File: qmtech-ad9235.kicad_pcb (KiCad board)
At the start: 4 copper layers, 60 x 45 mm, 49 parts

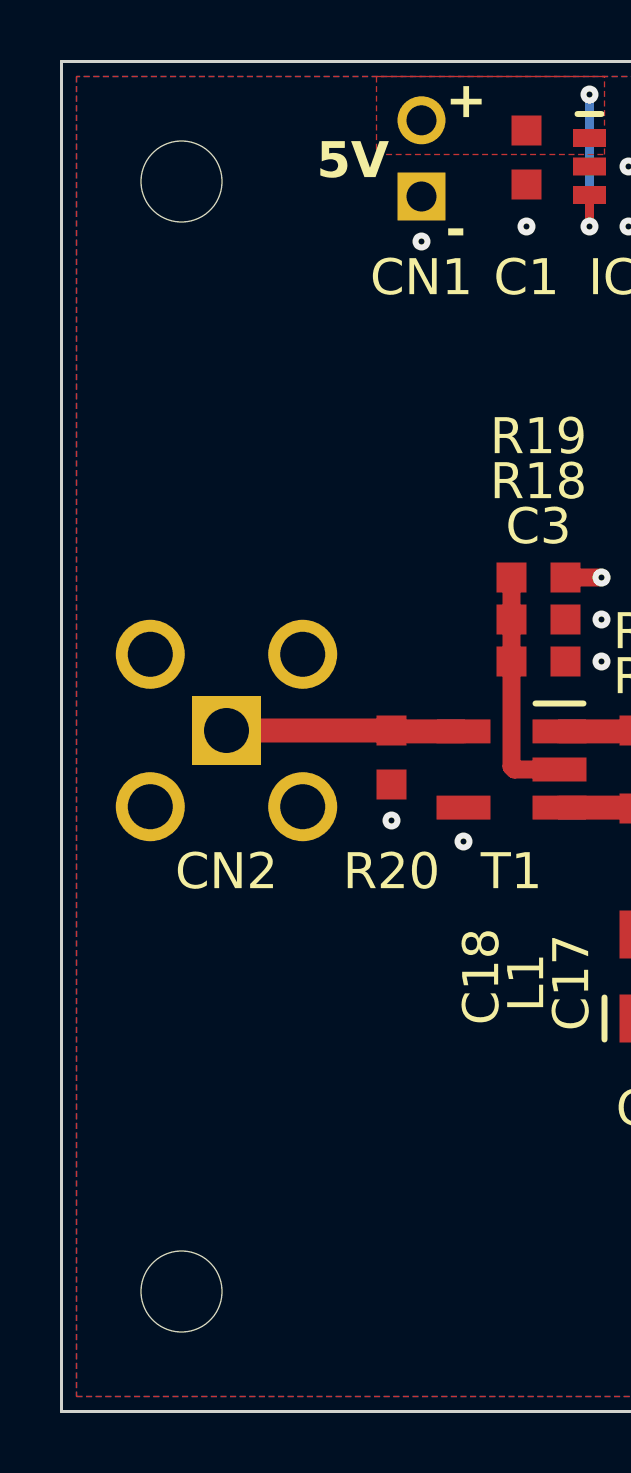
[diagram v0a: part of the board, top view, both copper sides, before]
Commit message: replace M25 with M3
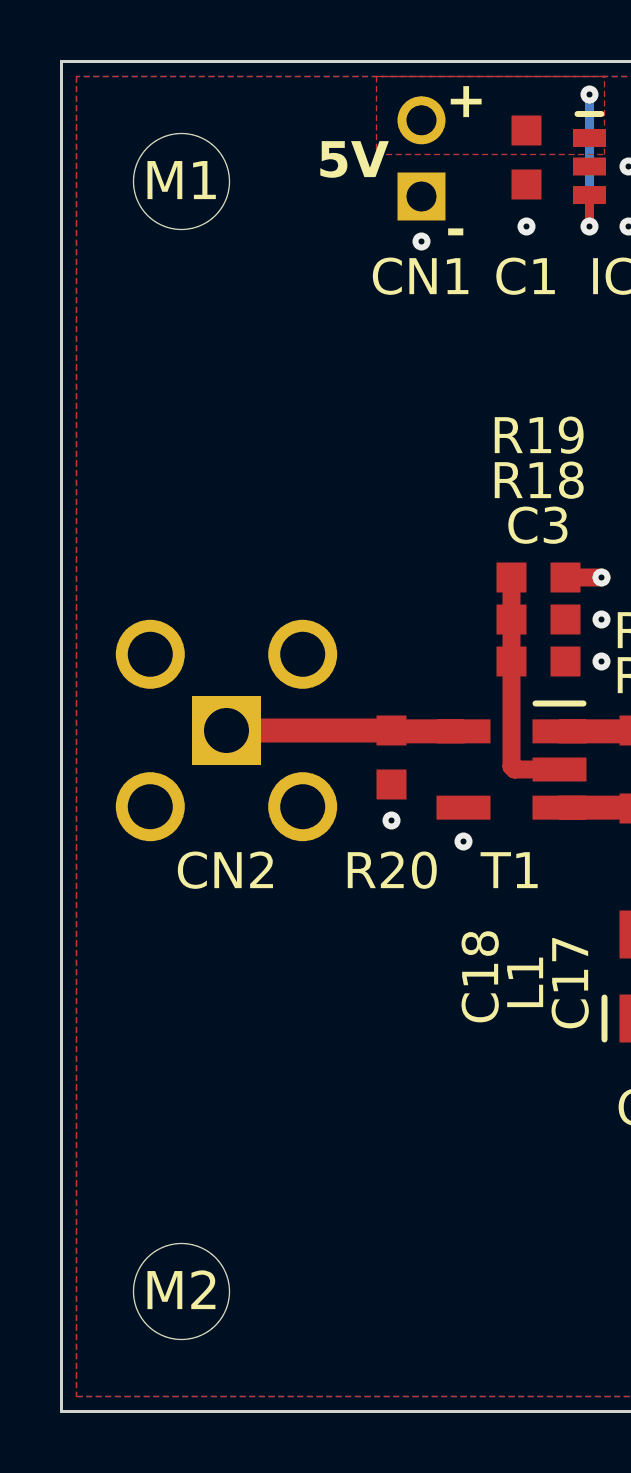
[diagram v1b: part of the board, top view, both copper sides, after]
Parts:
- M1, M2: footprint footprints:M25 -> footprints:M3
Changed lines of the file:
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@@
       (net 18 "GND"))
   )
-  (footprint "footprints:M25" (layer "F.Cu")
+  (footprint "footprints:M3" (layer "F.Cu")
     (at 72 52)
     (property "mpn" "hole")
     (clearance 1)
     (attr through_hole)
-    (fp_text reference "M1" (at 0 0) (layer "F.SilkS") hide
+    (fp_text reference "M1" (at 0 0) (layer "F.SilkS")
         (effects (font (size 1.27 1.27) (thickness 0.15)))
     )
@@
         (effects (font (size 1.27 1.27) (thickness 0.15)))
     )
-    (pad "" np_thru_hole circle (at 0 0) (size 2.7 2.7) (drill 2.7) (layers "*.Cu" "*.Mask"))
+    (pad "" np_thru_hole circle (at 0 0) (size 3.2 3.2) (drill 3.2) (layers "*.Cu" "*.Mask"))
   )
   (footprint "footprints:0603" (layer "F.Cu")
@@
       (net 18 "GND"))
   )
-  (footprint "footprints:M25" (layer "F.Cu")
+  (footprint "footprints:M3" (layer "F.Cu")
     (at 72 89)
     (property "mpn" "hole")
     (clearance 1)
     (attr through_hole)
-    (fp_text reference "M2" (at 0 0) (layer "F.SilkS") hide
+    (fp_text reference "M2" (at 0 0) (layer "F.SilkS")
         (effects (font (size 1.27 1.27) (thickness 0.15)))
     )
-    (fp_text value "" (at 0 0) (layer "F.SilkS") hide
+    (fp_text value "" (at 0 0) (layer "F.SilkS")
         (effects (font (size 1.27 1.27) (thickness 0.15)))
     )
-    (pad "" np_thru_hole circle (at 0 0) (size 2.7 2.7) (drill 2.7) (layers "*.Cu" "*.Mask"))
+    (pad "" np_thru_hole circle (at 0 0) (size 3.2 3.2) (drill 3.2) (layers "*.Cu" "*.Mask"))
   )
   (footprint "footprints:1x17" (layer "F.Cu")

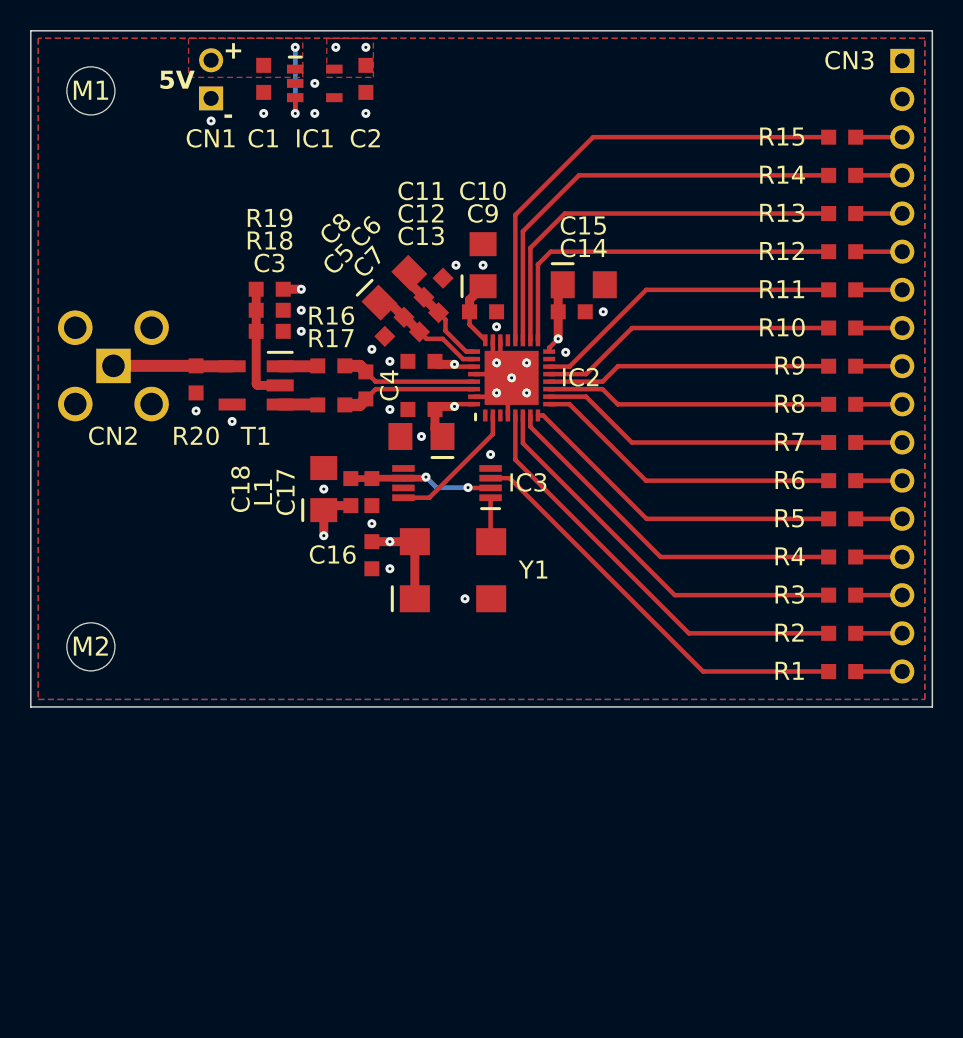
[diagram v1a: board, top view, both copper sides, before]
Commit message: reduce length of output traces
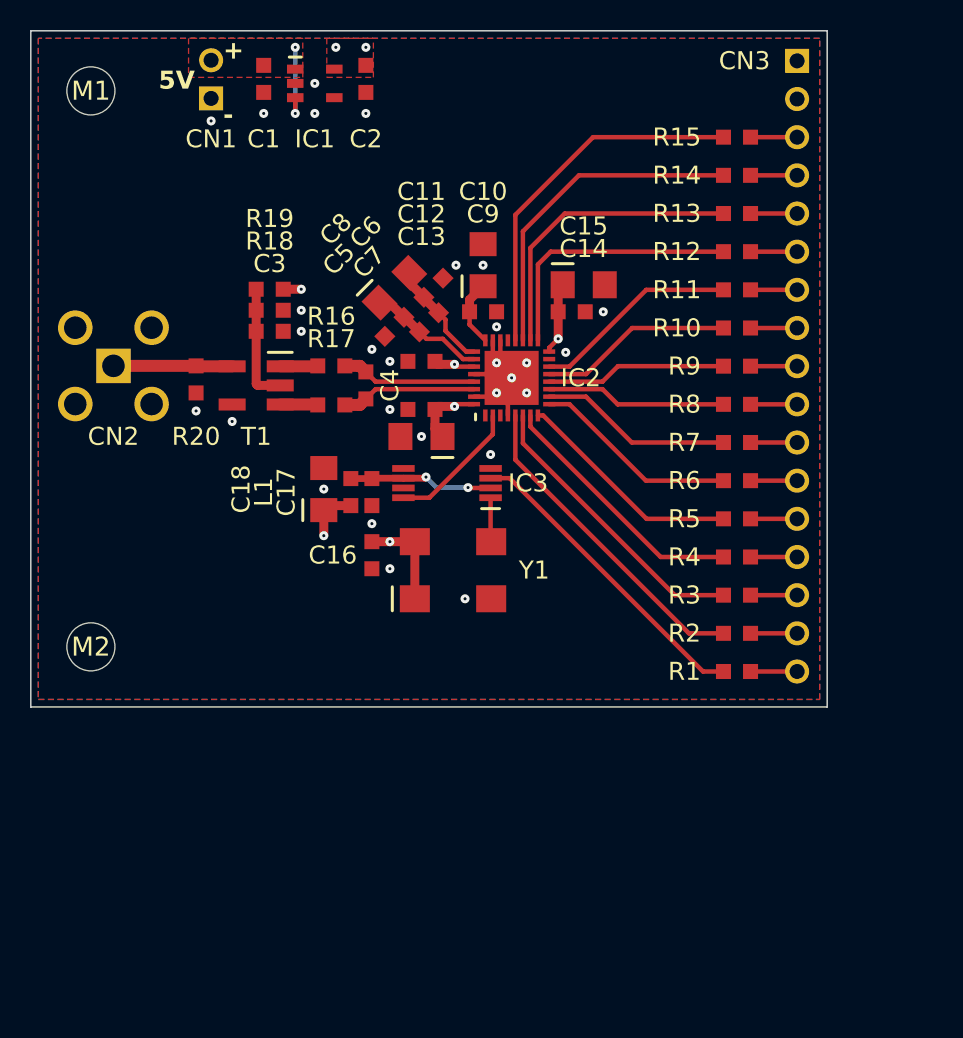
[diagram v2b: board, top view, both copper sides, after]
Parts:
- moved CN3 7.00 mm to (119.0, 50.0)
- moved R1 7.00 mm to (115.0, 90.6)
- moved R10 7.00 mm to (115.0, 67.8)
- moved R11 7.00 mm to (115.0, 65.2)
- moved R12 7.00 mm to (115.0, 62.7)
- moved R13 7.00 mm to (115.0, 60.2)
- moved R14 7.00 mm to (115.0, 57.6)
- moved R15 7.00 mm to (115.0, 55.1)
- moved R2 7.00 mm to (115.0, 88.1)
- moved R3 7.00 mm to (115.0, 85.6)
- moved R4 7.00 mm to (115.0, 83.0)
- moved R5 7.00 mm to (115.0, 80.5)
- moved R6 7.00 mm to (115.0, 77.9)
- moved R7 7.00 mm to (115.0, 75.4)
- moved R8 7.00 mm to (115.0, 72.9)
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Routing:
- net D6: track 19.0 -> 12.0 mm
- net Y1: track 27.8 -> 20.8 mm
- net D8: track 19.9 -> 12.9 mm
- net D7: track 19.0 -> 12.0 mm
- net D5: track 19.9 -> 12.9 mm
- net D4: track 20.7 -> 13.7 mm
- net D3: track 22.2 -> 15.2 mm
- net D2: track 24.2 -> 17.2 mm
- net D13: track 31.3 -> 24.3 mm
- net D12: track 29.1 -> 22.1 mm
- net D11: track 26.9 -> 19.9 mm
- net D10: track 24.8 -> 17.8 mm
- net D1: track 26.4 -> 19.4 mm
- net D0: track 28.6 -> 21.6 mm
- net D9: track 20.7 -> 13.7 mm
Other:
- board size 60 x 45 mm -> 53 x 45 mm

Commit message: improve AVDD and GND connections
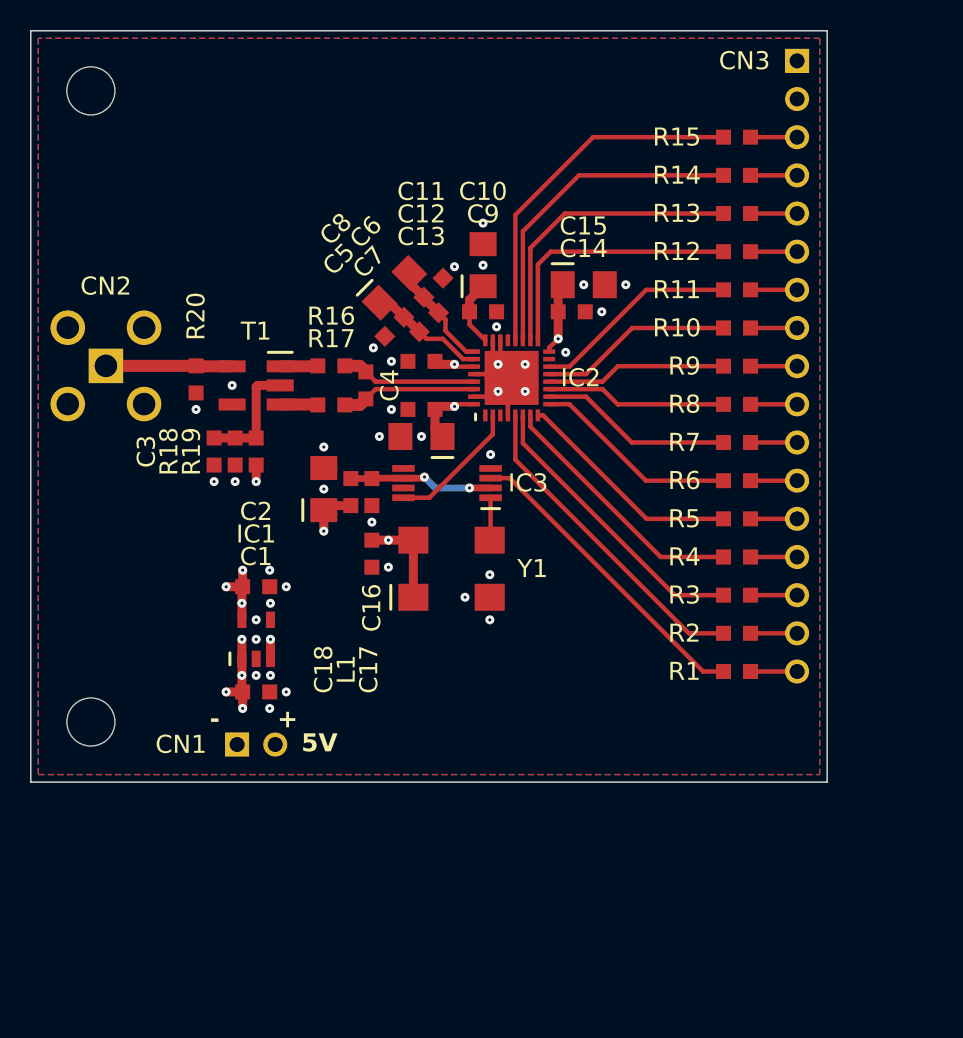
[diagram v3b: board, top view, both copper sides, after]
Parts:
- moved CN1 43.1 mm to (83.0, 95.5), turned to 0 degrees
- moved C1 40.8 mm to (83.0, 92.0), turned to 0 degrees
- moved IC1 37.2 mm to (83.0, 88.5), turned to 90 degrees
- moved C2 34.6 mm to (83.0, 85.0), turned to 0 degrees
- moved R18 10.8 mm to (83.0, 76.0), turned to 90 degrees
- moved R19 9.68 mm to (81.6, 76.0), turned to -90 degrees
- moved C3 8.81 mm to (80.2, 76.0), turned to -90 degrees
- moved M2 5.00 mm to (72.0, 94.0)
- moved CN2 0.50 mm to (73.0, 70.3)
- moved Y1 0.14 mm to (96.0, 83.8)
- moved C16 0.10 mm to (90.7, 82.8)
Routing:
- net AVDD: track 18.9 -> 22.9 mm, vias 7 -> 8
- net 5V: track 5.45 -> 7.02 mm, vias 2 -> 5
- net INPUT: track 7.91 -> 8.41 mm
- net GND: vias 28 -> 38
- added copper zone on In2.Cu, net 5V
- added copper zone on In2.Cu, net AVDD
- added copper zone on In2.Cu, net DVDD
- added copper zone on In1.Cu, net GND
- removed copper zone on F.Cu, net 5V
- removed copper zone on F.Cu, net AVDD
- removed copper zone on In1.Cu, net AVDD
- removed copper zone on In1.Cu, net DVDD
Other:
- board size 53 x 45 mm -> 53 x 50 mm

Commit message: replace 1x17 with 2x25
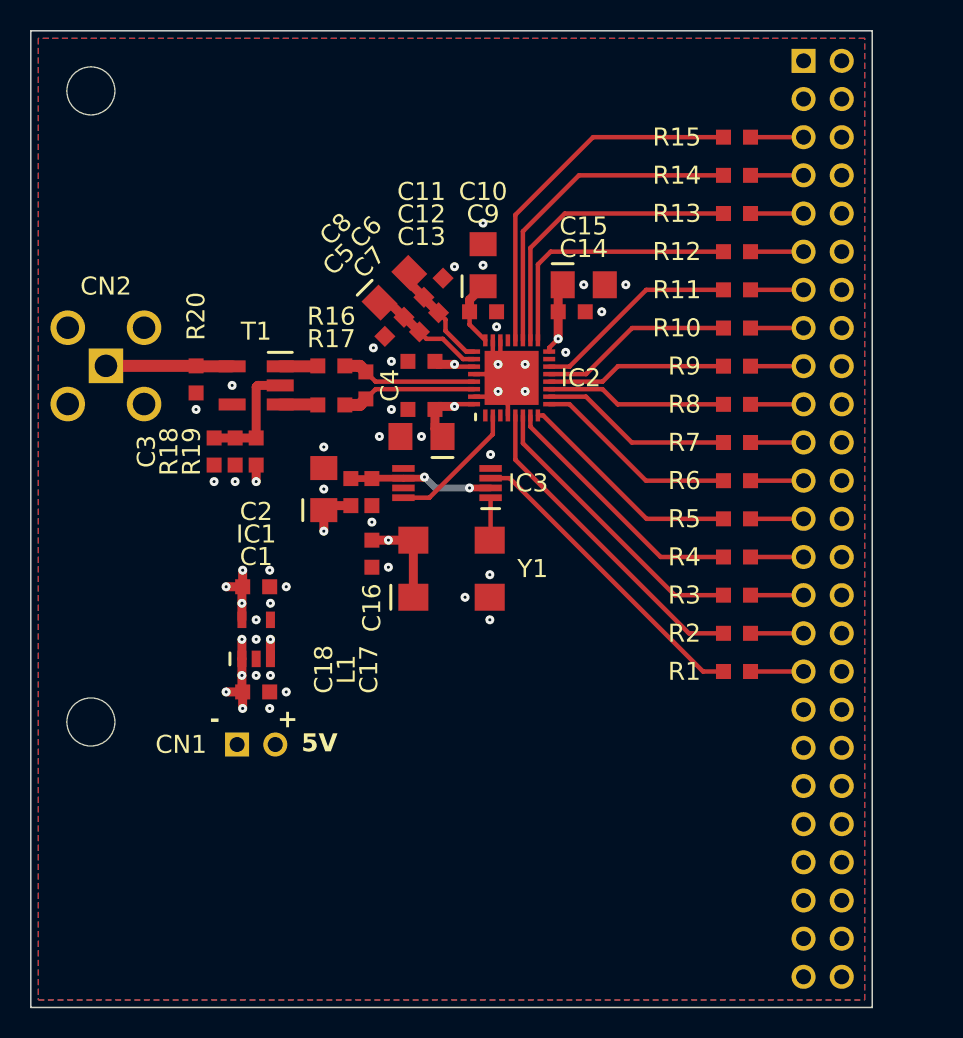
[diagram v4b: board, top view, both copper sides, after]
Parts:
- CN3: footprint footprints:1x17 -> footprints:2x25; moved to B.Cu
- moved CN3 1.70 mm to (120.7, 50.0)
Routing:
- net W9: track 3.00 -> 3.53 mm
- net W8: track 3.00 -> 3.53 mm
- net W7: track 3.00 -> 3.53 mm
- net W6: track 3.00 -> 3.53 mm
- net W5: track 3.00 -> 3.53 mm
- net W4: track 3.00 -> 3.53 mm
- net W3: track 3.00 -> 3.53 mm
- net W2: track 3.00 -> 3.53 mm
- net W15: track 3.00 -> 3.53 mm
- net W14: track 3.00 -> 3.53 mm
- net W13: track 3.00 -> 3.53 mm
- net W12: track 3.00 -> 3.53 mm
- net W11: track 3.00 -> 3.53 mm
- net W10: track 3.00 -> 3.53 mm
- net W1: track 3.00 -> 3.53 mm
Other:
- board size 53 x 50 mm -> 56 x 65 mm

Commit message: add DVDD regulator
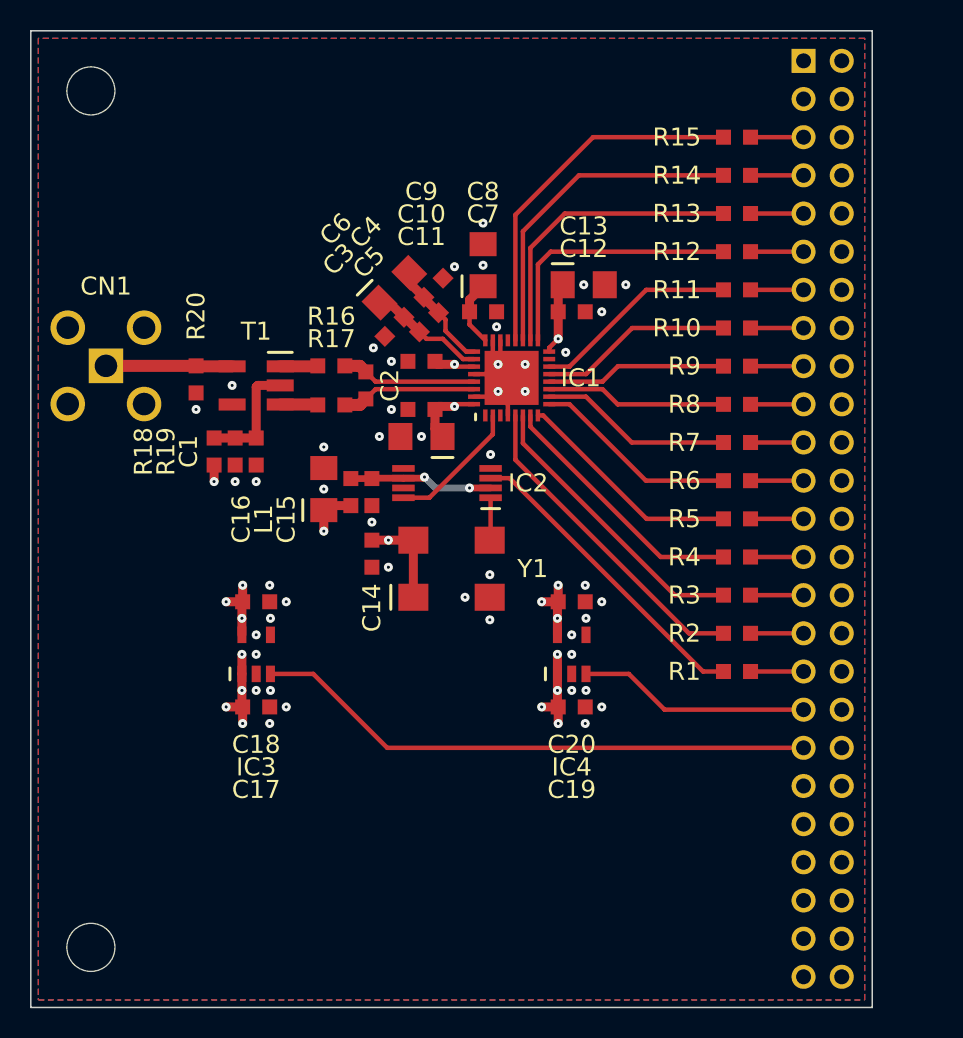
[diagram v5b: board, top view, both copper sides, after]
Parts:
- removed the CN1 at (83.0, 95.5)
- added C19: , footprints:0603, F.Cu at (104.0, 93.0)
- added C20: , footprints:0603, F.Cu at (104.0, 86.0)
- added IC4: , footprints:SOT23, F.Cu at (104.0, 89.5)
- moved M2 15.0 mm to (72.0, 109.0)
- moved C1 2.80 mm to (83.0, 76.0)
- moved R18 2.80 mm to (80.2, 76.0)
- moved C17 1.00 mm to (83.0, 93.0)
- moved C18 1.00 mm to (83.0, 86.0)
- moved IC3 1.00 mm to (83.0, 89.5)
- renumbered C3 to C1, C12 to C10, C13 to C11, C14 to C12, C15 to C13, C16 to C14, C17 to C15, C18 to C16, C1 to C17, C2 to C18, C4 to C2, C5 to C3, C6 to C4, C7 to C5, C8 to C6, C9 to C7, C10 to C8, C11 to C9, CN2 to CN1, CN3 to CN2, IC2 to IC1, IC3 to IC2, IC1 to IC3
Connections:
- CN2 pad 2: (no net) -> GND
- CN2 pad 3: DVDD -> (no net)
- CN2 pad 35: (no net) -> DEN
- CN2 pad 37: (no net) -> AEN
- CN2 pad 47: (no net) -> GND
- CN2 pad 48: (no net) -> GND
- CN2 pad 49: (no net) -> 5V
- CN2 pad 50: (no net) -> 5V
- IC3 pad 3: 5V -> AEN
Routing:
- net AEN: track 0.00 -> 37.5 mm
- net DEN: track 0.00 -> 15.5 mm
- net 5V: track 7.02 -> 11.4 mm, vias 5 -> 8
- net DVDD: track 4.82 -> 9.24 mm, vias 1 -> 4
- net GND: vias 38 -> 47
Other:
- board text removed: "+"
- board text removed: "-"
- board text removed: "5V"
